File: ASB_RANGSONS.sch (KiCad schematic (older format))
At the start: 24 parts, among them P1 MMD_FRC_34PIN, P10 SSD_FRC_20PIN, P2 CONN _1_20, P3 CONN_21_40, P4 CONN_41_60, P5 CONN_61_80, P6 MMD_ROW, P7 PWR_5V, P8 ETH_CON, P9 PWR_12V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

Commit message: MMD_CONTROL_IS_MODIFIED
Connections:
- wire segments 232 -> 231
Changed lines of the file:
@@
 Sheet 1 1
 Title ""
-Date "17 mar 2015"
+Date "18 mar 2015"
 Rev ""
 Comp ""
@@
 	1    0    0    -1
 $EndComp
-NoConn ~ 4950 6500
+NoConn ~ 4150 6500
 NoConn ~ 4950 5700
 Text Label 5100 4900 0    39   ~ 0
@@
 Text Label 1650 6750 0    39   ~ 0
 33
-Text Label 4100 6650 0    39   ~ 0
+Text Label 5050 6500 0    39   ~ 0
 34
 Text Label 9050 1400 0    39   ~ 0
@@
 	4050 6400 4150 6400
 Wire Wire Line
-	4150 6500 4100 6500
-Wire Wire Line
-	4100 6500 4100 6750
-Wire Wire Line
 	4950 4900 5300 4900
 Wire Wire Line
@@
 NoConn ~ 7350 1800
 NoConn ~ 7350 1900
+Wire Wire Line
+	4950 6500 5300 6500
 $EndSCHEMATC

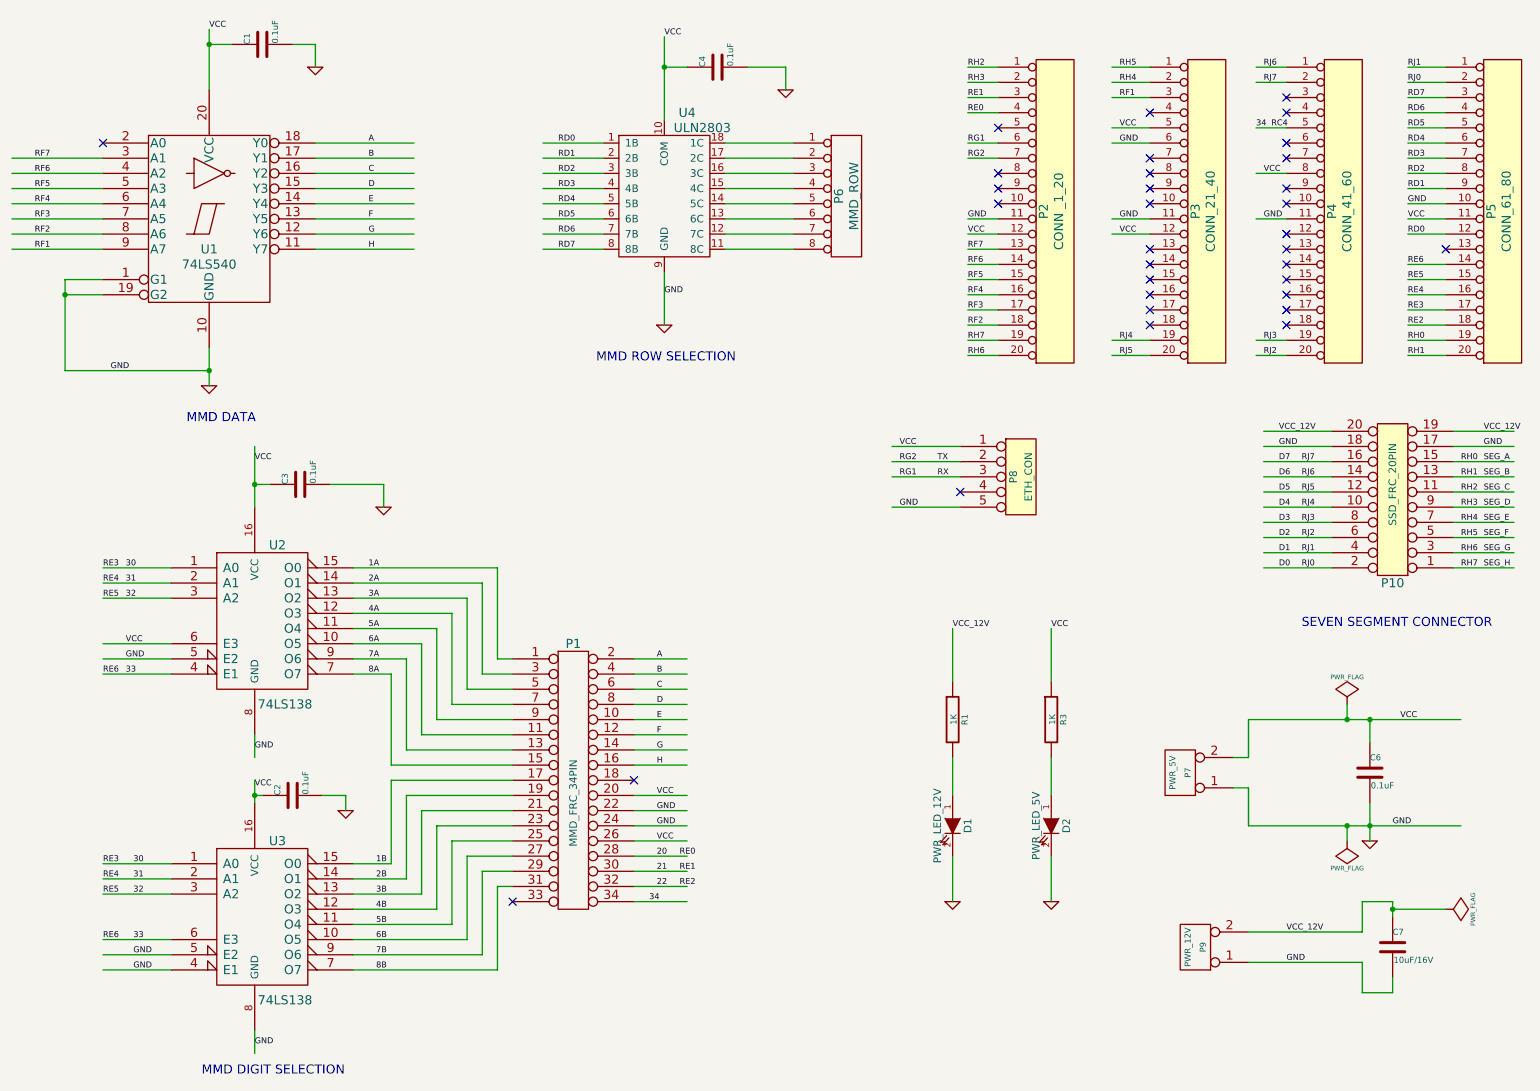
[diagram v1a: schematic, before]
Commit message: Data lines modified as per led latch schematic
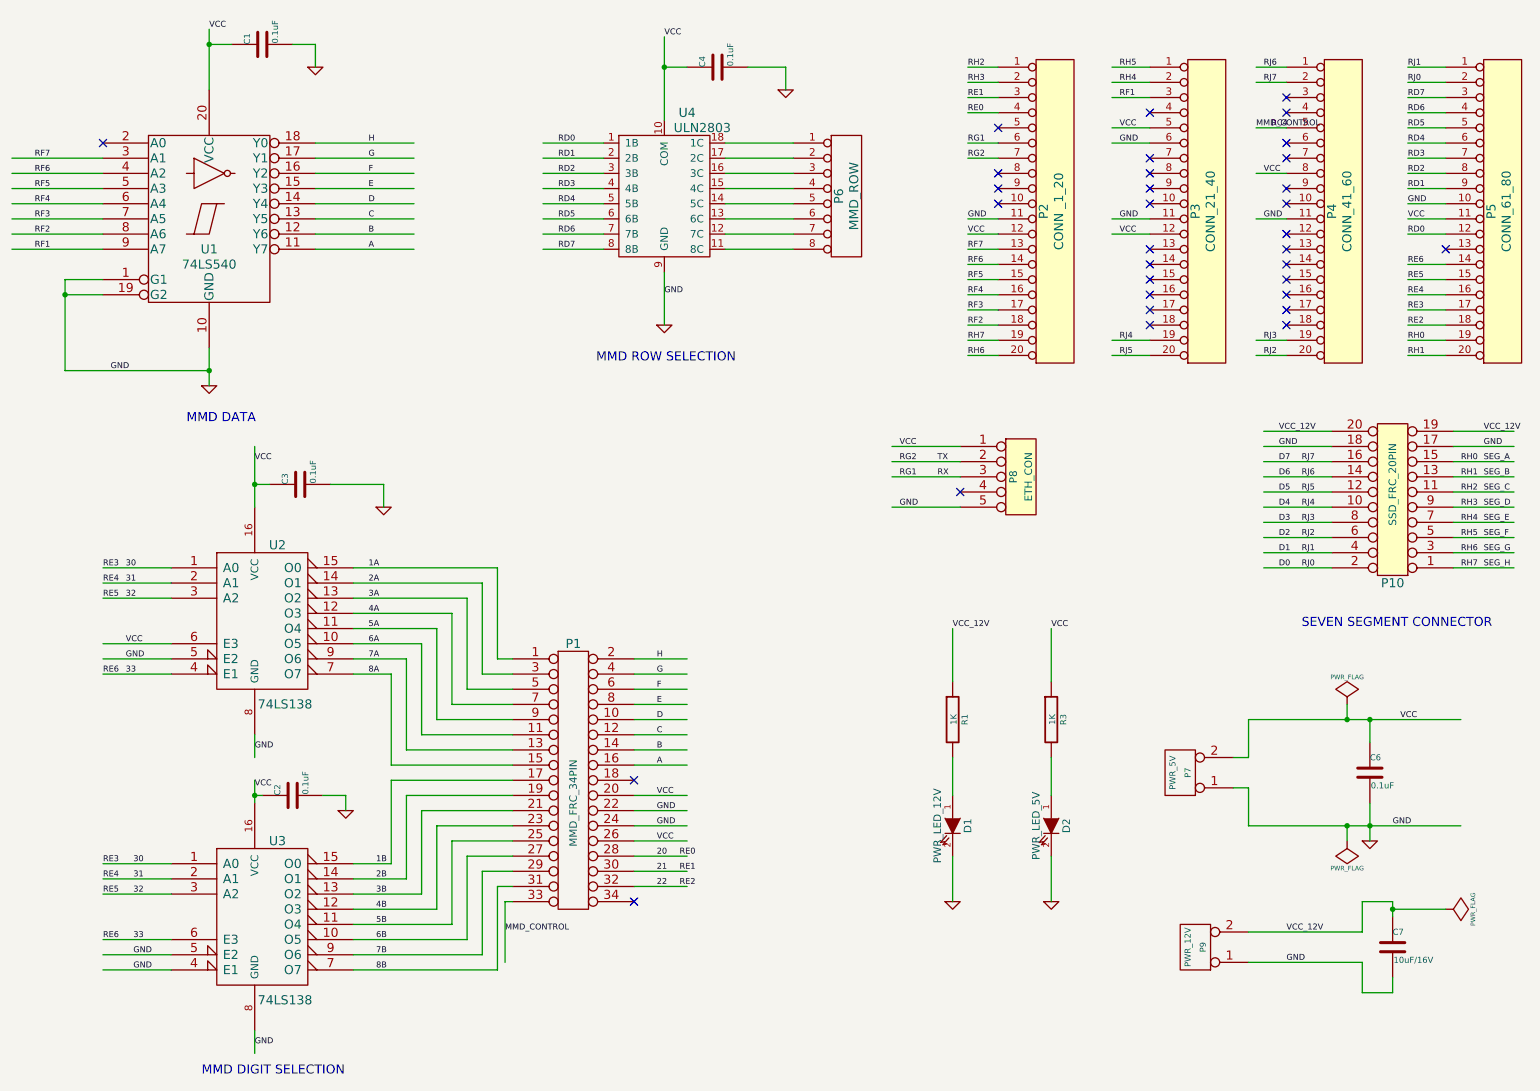
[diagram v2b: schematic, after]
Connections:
- net labels added: MMD_CONTROL
- net labels removed: 34
- wire segments 231 -> 232
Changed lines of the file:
@@
 Sheet 1 1
 Title ""
-Date "18 mar 2015"
+Date "19 mar 2015"
 Rev ""
 Comp ""
@@
 	1    0    0    -1
 $EndComp
-NoConn ~ 4150 6500
+NoConn ~ 4950 6500
 NoConn ~ 4950 5700
 Text Label 5100 4900 0    39   ~ 0
+H
+Text Label 5100 5000 0    39   ~ 0
+G
+Text Label 5100 5100 0    39   ~ 0
+F
+Text Label 5100 5200 0    39   ~ 0
+E
+Text Label 5100 5300 0    39   ~ 0
+D
+Text Label 5100 5400 0    39   ~ 0
+C
+Text Label 5100 5500 0    39   ~ 0
+B
+Text Label 5100 5600 0    39   ~ 0
 A
-Text Label 5100 5000 0    39   ~ 0
+Text Label 3200 1500 0    39   ~ 0
+H
+Text Label 3200 1600 0    39   ~ 0
+G
+Text Label 3200 1700 0    39   ~ 0
+F
+Text Label 3200 1800 0    39   ~ 0
+E
+Text Label 3200 1900 0    39   ~ 0
+D
+Text Label 3200 2000 0    39   ~ 0
+C
+Text Label 3200 2100 0    39   ~ 0
 B
-Text Label 5100 5100 0    39   ~ 0
-C
-Text Label 5100 5200 0    39   ~ 0
-D
-Text Label 5100 5300 0    39   ~ 0
-E
-Text Label 5100 5400 0    39   ~ 0
-F
-Text Label 5100 5500 0    39   ~ 0
-G
-Text Label 5100 5600 0    39   ~ 0
-H
-Text Label 3200 1500 0    39   ~ 0
+Text Label 3200 2200 0    39   ~ 0
 A
-Text Label 3200 1600 0    39   ~ 0
-B
-Text Label 3200 1700 0    39   ~ 0
-C
-Text Label 3200 1800 0    39   ~ 0
-D
-Text Label 3200 1900 0    39   ~ 0
-E
-Text Label 3200 2000 0    39   ~ 0
-F
-Text Label 3200 2100 0    39   ~ 0
-G
-Text Label 3200 2200 0    39   ~ 0
-H
 Text Label 5100 5800 0    39   ~ 0
 VCC
@@
 Text Label 1650 6750 0    39   ~ 0
 33
-Text Label 5050 6500 0    39   ~ 0
-34
-Text Label 9050 1400 0    39   ~ 0
-34
+Text Label 4100 6700 0    39   ~ 0
+MMD_CONTROL
 $Comp
 L ULN2803 U4
@@
 NoConn ~ 7350 1900
 Wire Wire Line
-	4950 6500 5300 6500
+	4150 6500 4100 6500
+Wire Wire Line
+	4100 6500 4100 6900
+Text Label 9050 1400 0    39   ~ 0
+MMD_CONTROL
 $EndSCHEMATC
